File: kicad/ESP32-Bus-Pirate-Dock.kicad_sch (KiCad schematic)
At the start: 25 parts, among them CN1 HX25418-10WA, J1 Conn_01x10V, J2 Conn_01x22, J3 Conn_01x22, J4 Conn_02x03, J5 Conn_01x22, J6 Conn_01x22, J7 Conn_01x22, U1 ESP32-S3-DEVKITC-1-N8R2, U2 LDL1117S33R, U3 FXMA108

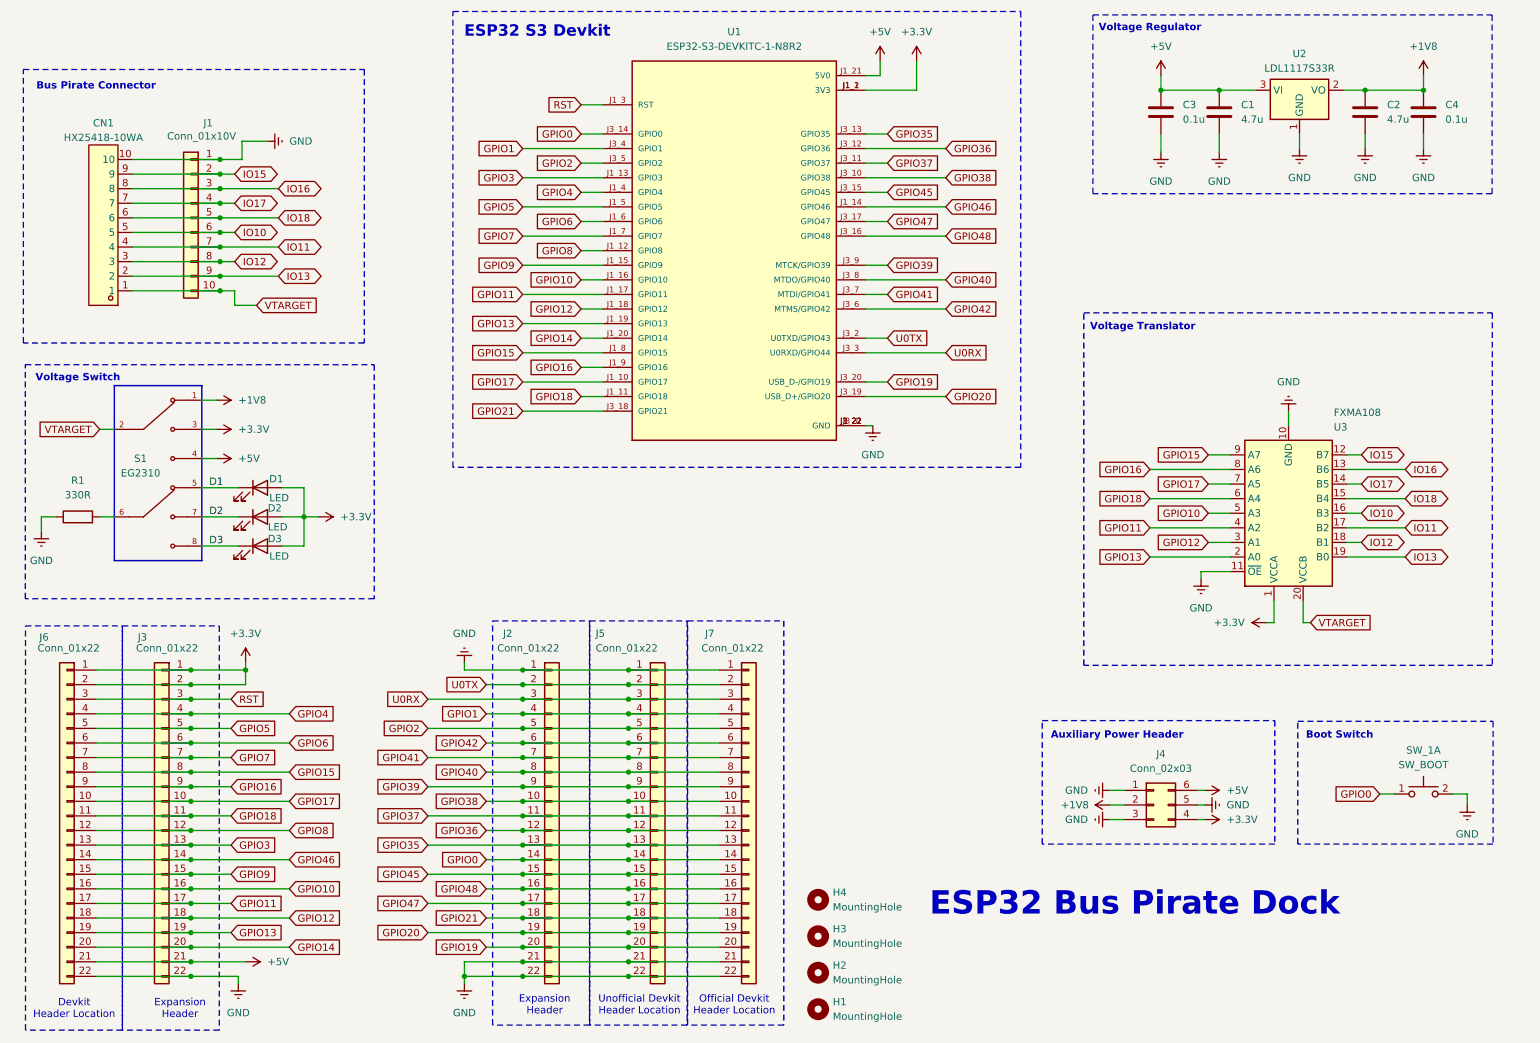
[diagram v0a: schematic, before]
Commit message: Wired up LSF0108 Voltage Translator
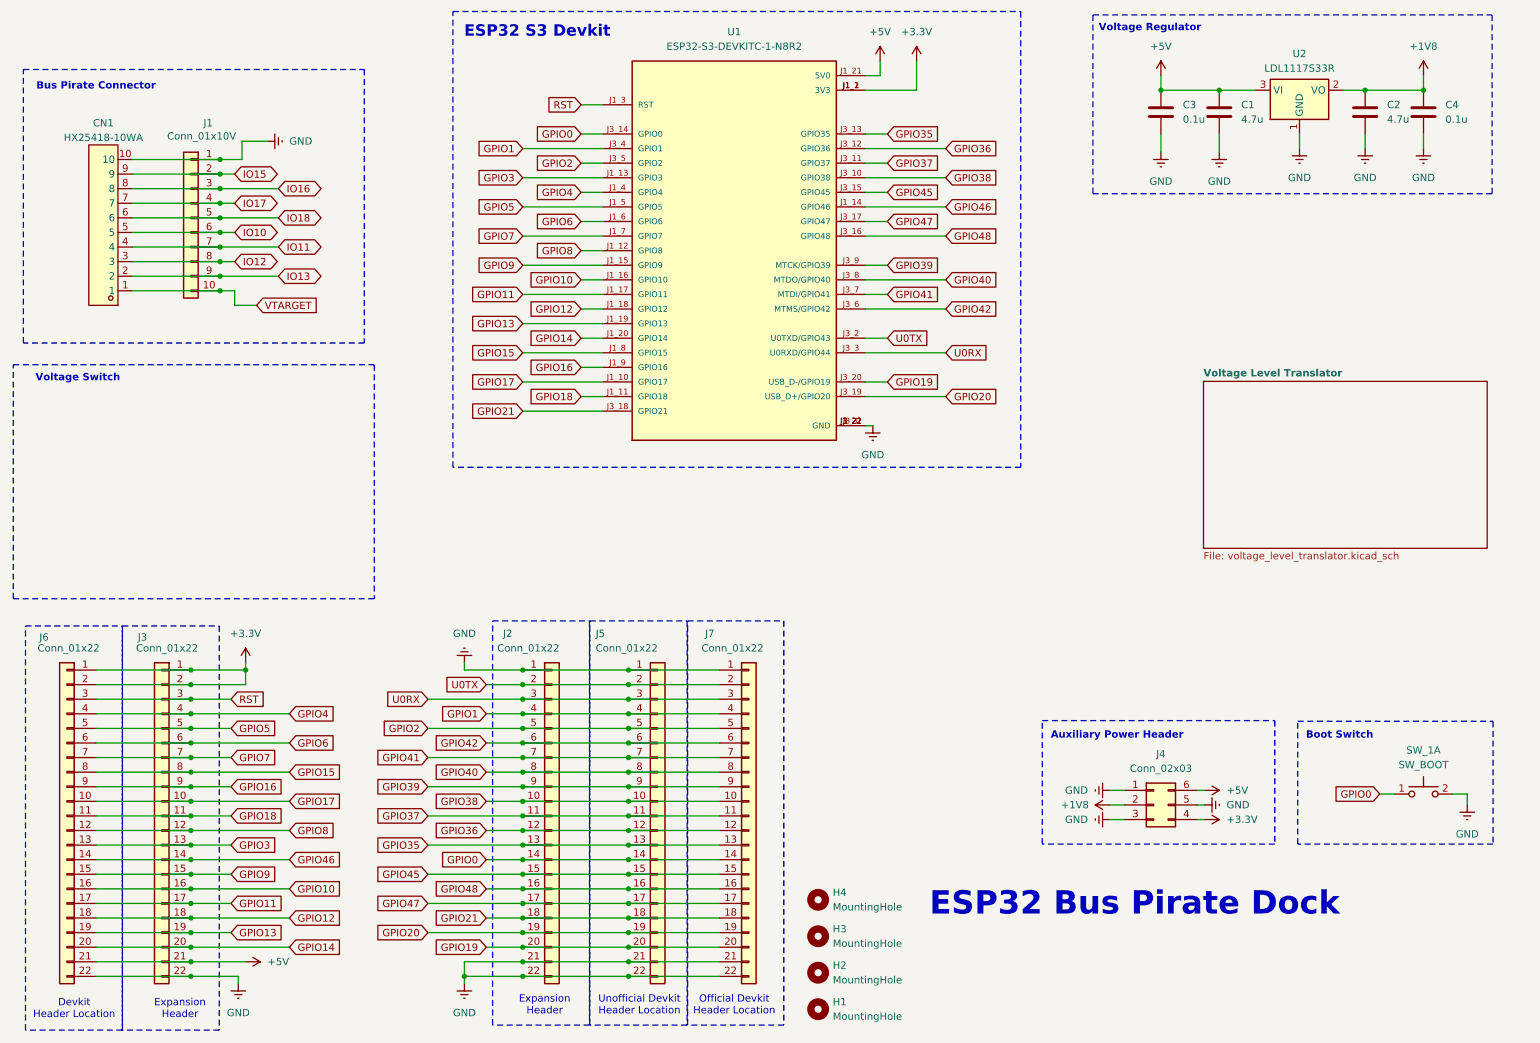
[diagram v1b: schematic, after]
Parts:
- removed D1, D2, D3: LED, LED_SMD:LED_0805_2012Metric, symbol Device:LED
- removed R1: 330R, Resistor_SMD:R_0805_2012Metric, symbol Device:R
- removed S1: EG2310, EG2310:SW_EG2310, symbol EG2310:EG2310
- removed U3: FXMA108, Package_DFN_QFN:WQFN-20-1EP_2.5x4.5mm_P0.5mm_EP1x2.9mm, symbol Logic_LevelTranslator:FXMA108
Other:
- added sheet Voltage Level Translator (voltage_level_translator.kicad_sch)
- note removed: "Voltage Translator"

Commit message: Added LSF1080 PCB placeholders
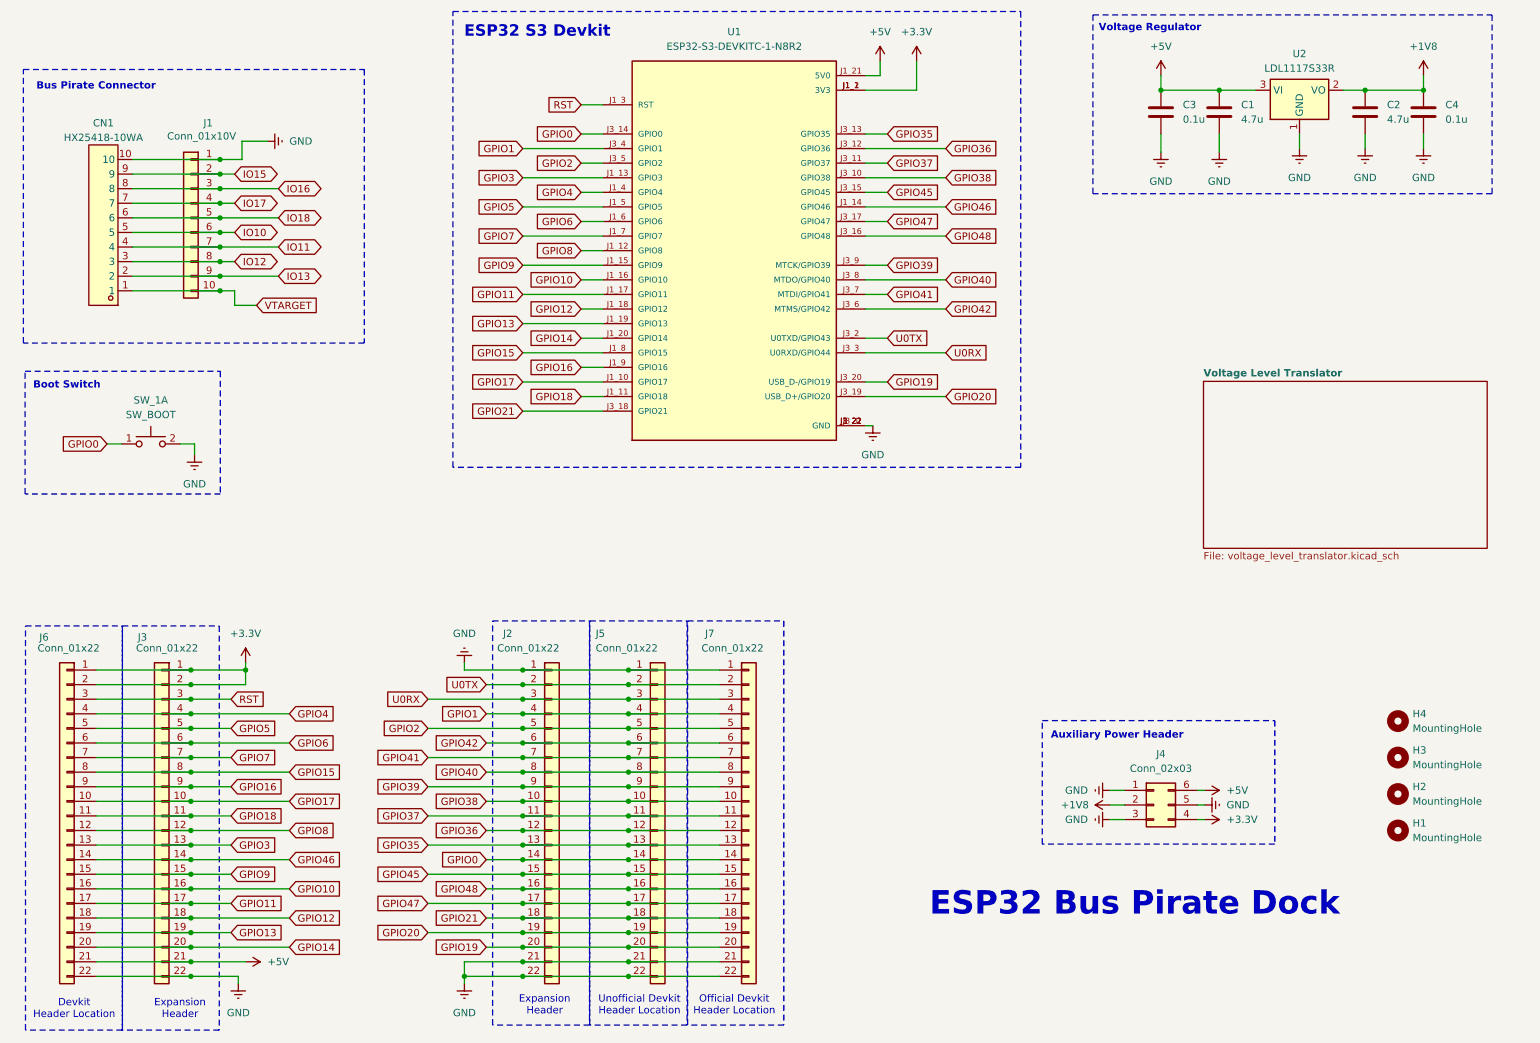
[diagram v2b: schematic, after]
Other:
- note removed: "Voltage Switch"
- moved on the sheet: H1, H2, H3, H4, SW_1A
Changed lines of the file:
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@@
 	)
 	(rectangle
-		(start 19.875 78.28)
-		(end 82.72 119.03)
-		(stroke
-			(width 0)
-			(type dash)
-			(color 132 132 0 1)
-		)
-		(fill
-			(type none)
-		)
-	)
-	(rectangle
 		(start 21.995 123.77)
 		(end 38.87 194.145)
@@
 	)
 	(rectangle
-		(start 243.54 140.375)
-		(end 277.54 161.75)
+		(start 21.925 79.415)
+		(end 55.925 100.79)
 		(stroke
 			(width 0)
@@
 	(text "Boot Switch"
 		(exclude_from_sim no)
-		(at 250.825 142.875 0)
+		(at 29.21 81.915 0)
 		(effects
 			(font
@@
 		)
 	)
-	(text "Voltage Switch"
-		(exclude_from_sim no)
-		(at 31.115 80.645 0)
-		(effects
-			(font
-				(size 1.27 1.27)
-				(thickness 0.254)
-				(bold yes)
-				(color 132 132 0 1)
-			)
-		)
-	)
 	(text "ESP32 S3 Devkit"
 		(exclude_from_sim no)
@@
 	(wire
 		(pts
-			(xy 257.81 153.035) (xy 260.35 153.035)
+			(xy 36.195 92.075) (xy 38.735 92.075)
 		)
 		(stroke
@@
 	(wire
 		(pts
-			(xy 273.05 154.94) (xy 273.05 153.035)
+			(xy 51.435 93.98) (xy 51.435 92.075)
 		)
 		(stroke
@@
 	(wire
 		(pts
-			(xy 273.05 153.035) (xy 270.51 153.035)
+			(xy 51.435 92.075) (xy 48.895 92.075)
 		)
 		(stroke
@@
 	(global_label "GPIO0"
 		(shape input)
-		(at 257.81 153.035 180)
+		(at 36.195 92.075 180)
 		(fields_autoplaced yes)
 		(effects
@@
 		)
 		(property "Intersheetrefs" "${INTERSHEET_REFS}"
-			(at 249.14 153.035 0)
+			(at 27.525 92.075 0)
 			(effects
 				(font
@@
 	(symbol
 		(lib_id "power:Earth")
-		(at 273.05 154.94 0)
+		(at 51.435 93.98 0)
 		(unit 1)
 		(exclude_from_sim no)
@@
 		(fields_autoplaced yes)
 		(property "Reference" "#PWR011"
-			(at 273.05 161.29 0)
+			(at 51.435 100.33 0)
 			(effects
 				(font
@@
 		)
 		(property "Value" "GND"
-			(at 273.05 160.02 0)
+			(at 51.435 99.06 0)
 			(effects
 				(font
@@
 		)
 		(property "Footprint" ""
-			(at 273.05 154.94 0)
+			(at 51.435 93.98 0)
 			(effects
 				(font
@@
 		)
 		(property "Datasheet" "~"
-			(at 273.05 154.94 0)
+			(at 51.435 93.98 0)
 			(effects
 				(font
@@
 		)
 		(property "Description" "Power symbol creates a global label with name \"Earth\""
-			(at 273.05 154.94 0)
+			(at 51.435 93.98 0)
 			(effects
 				(font
@@
 	(symbol
 		(lib_id "Mechanical:MountingHole")
-		(at 160.02 184.15 0)
+		(at 260.985 153.035 0)
 		(unit 1)
 		(exclude_from_sim no)
@@
 		(dnp no)
 		(property "Reference" "H2"
-			(at 162.56 182.8799 0)
+			(at 263.525 151.7649 0)
 			(effects
 				(font
@@
 		)
 		(property "Value" "MountingHole"
-			(at 162.56 185.4199 0)
+			(at 263.525 154.3049 0)
 			(effects
 				(font
@@
 		)
 		(property "Footprint" "MountingHole:MountingHole_3.2mm_M3_DIN965_Pad_TopBottom"
-			(at 160.02 184.15 0)
+			(at 260.985 153.035 0)
 			(effects
 				(font
@@
 		)
 		(property "Datasheet" "~"
-			(at 160.02 184.15 0)
+			(at 260.985 153.035 0)
 			(effects
 				(font
@@
 		)
 		(property "Description" "Mounting Hole without connection"
-			(at 160.02 184.15 0)
+			(at 260.985 153.035 0)
 			(effects
 				(font
@@
 	(symbol
 		(lib_id "Switch:SW_Push_Dual_x2")
-		(at 265.43 153.035 0)
+		(at 43.815 92.075 0)
 		(unit 1)
 		(exclude_from_sim no)
@@
 		(dnp no)
 		(property "Reference" "SW_1"
-			(at 265.43 145.415 0)
+			(at 43.815 84.455 0)
 			(effects
 				(font
@@
 		)
 		(property "Value" "SW_BOOT"
-			(at 265.43 147.955 0)
+			(at 43.815 86.995 0)
 			(effects
 				(font
@@
 		)
 		(property "Footprint" "Button_Switch_SMD:SW_SPST_PTS645Sx43SMTR92"
-			(at 265.43 147.955 0)
+			(at 43.815 86.995 0)
 			(effects
 				(font
@@
 		)
 		(property "Datasheet" "~"
-			(at 265.43 147.955 0)
+			(at 43.815 86.995 0)
 			(effects
 				(font
@@
 		)
 		(property "Description" "Push button switch, generic, separate symbols, four pins"
-			(at 265.43 153.035 0)
+			(at 43.815 92.075 0)
 			(effects
 				(font
@@
 	(symbol
 		(lib_id "Mechanical:MountingHole")
-		(at 160.02 171.45 0)
+		(at 260.985 140.335 0)
 		(unit 1)
 		(exclude_from_sim no)
@@
 		(dnp no)
 		(property "Reference" "H4"
-			(at 162.56 170.1799 0)
+			(at 263.525 139.0649 0)
 			(effects
 				(font
@@
 		)
 		(property "Value" "MountingHole"
-			(at 162.56 172.7199 0)
+			(at 263.525 141.6049 0)
 			(effects
 				(font
@@
 		)
 		(property "Footprint" "MountingHole:MountingHole_3.2mm_M3_DIN965_Pad_TopBottom"
-			(at 160.02 171.45 0)
+			(at 260.985 140.335 0)
 			(effects
 				(font
@@
 		)
 		(property "Datasheet" "~"
-			(at 160.02 171.45 0)
+			(at 260.985 140.335 0)
 			(effects
 				(font
@@
 		)
 		(property "Description" "Mounting Hole without connection"
-			(at 160.02 171.45 0)
+			(at 260.985 140.335 0)
 			(effects
 				(font
@@
 	(symbol
 		(lib_id "Mechanical:MountingHole")
-		(at 160.02 177.8 0)
+		(at 260.985 146.685 0)
 		(unit 1)
 		(exclude_from_sim no)
@@
 		(dnp no)
 		(property "Reference" "H3"
-			(at 162.56 176.5299 0)
+			(at 263.525 145.4149 0)
 			(effects
 				(font
@@
 		)
 		(property "Value" "MountingHole"
-			(at 162.56 179.0699 0)
+			(at 263.525 147.9549 0)
 			(effects
 				(font
@@
 		)
 		(property "Footprint" "MountingHole:MountingHole_3.2mm_M3_DIN965_Pad_TopBottom"
-			(at 160.02 177.8 0)
+			(at 260.985 146.685 0)
 			(effects
 				(font
@@
 		)
 		(property "Datasheet" "~"
-			(at 160.02 177.8 0)
+			(at 260.985 146.685 0)
 			(effects
 				(font
@@
 		)
 		(property "Description" "Mounting Hole without connection"
-			(at 160.02 177.8 0)
+			(at 260.985 146.685 0)
 			(effects
 				(font
@@
 	(symbol
 		(lib_id "Mechanical:MountingHole")
-		(at 160.02 190.5 0)
+		(at 260.985 159.385 0)
 		(unit 1)
 		(exclude_from_sim no)
@@
 		(dnp no)
 		(property "Reference" "H1"
-			(at 162.56 189.2299 0)
+			(at 263.525 158.1149 0)
 			(effects
 				(font
@@
 		)
 		(property "Value" "MountingHole"
-			(at 162.56 191.7699 0)
+			(at 263.525 160.6549 0)
 			(effects
 				(font
@@
 		)
 		(property "Footprint" "MountingHole:MountingHole_3.2mm_M3_DIN965_Pad_TopBottom"
-			(at 160.02 190.5 0)
+			(at 260.985 159.385 0)
 			(effects
 				(font
@@
 		)
 		(property "Datasheet" "~"
-			(at 160.02 190.5 0)
+			(at 260.985 159.385 0)
 			(effects
 				(font
@@
 		)
 		(property "Description" "Mounting Hole without connection"
-			(at 160.02 190.5 0)
+			(at 260.985 159.385 0)
 			(effects
 				(font

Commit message: Experimented with wiring
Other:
- note added: "2.54mm Headers"
- note added: "Mounting Holes"
- moved on the sheet: CN1, H1, H2, H3, H4, J1, J2, J3, J4, J5, J6, J7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

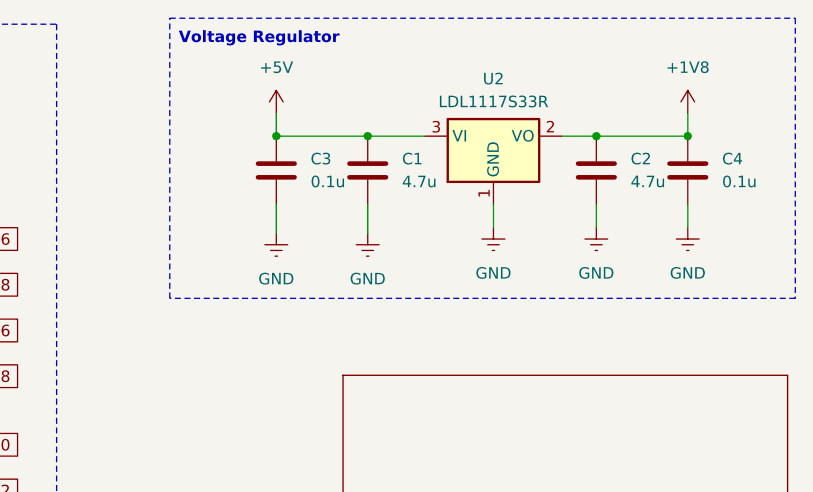
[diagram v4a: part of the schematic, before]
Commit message: Changed LDO to TLV75518
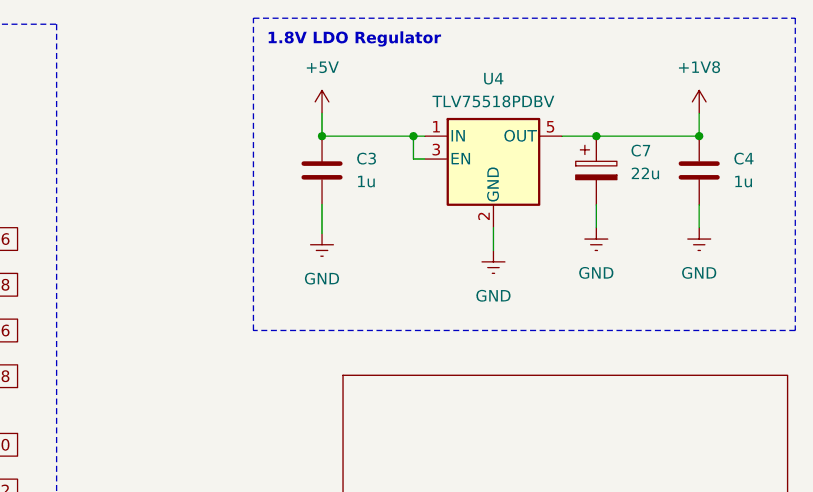
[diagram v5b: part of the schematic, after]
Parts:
- removed C1, C2: 4.7u, Capacitor_SMD:C_0805_2012Metric, symbol Device:C
- removed U2: LDL1117S33R, Package_TO_SOT_SMD:SOT-223-3_TabPin2, symbol Regulator_Linear:AMS1117-1.8
- added C7: 22u, Capacitor_SMD:CP_Elec_5x4.5, symbol Device:C_Polarized
- added U4: TLV75518PDBV, Package_TO_SOT_SMD:SOT-23-5, symbol Regulator_Linear:TLV75518PDBV
- C3, C4: value 0.1u -> 1u
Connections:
- net +1V8: now also C7.1, U4.5 (OUT)
- net +5V: now also U4.1 (IN), U4.3 (EN)
- net GND: now also C7.2, U4.2 (GND)
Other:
- note added: "1.8V LDO Regulator"
- note removed: "Voltage Regulator"
- moved on the sheet: C3, C4
